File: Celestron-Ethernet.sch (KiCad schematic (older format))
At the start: 59 parts, among them J1 USB_B_Micro, J2 6P6C, J3 RJ45_Abracon_ARJP11A-MASA-B-A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, SW1 SW_SPDT, U1 ATmega32U4-AU, U2 LP2985-5.0, U3 LP2985-3.3, U4 W5500, Y1 16MHz, Y2 25MHz

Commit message: Initial routing
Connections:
- net labels added: 12V
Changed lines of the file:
@@
 Wire Wire Line
 	1750 2450 2550 2450
+Text Label 4450 5150 0    50   ~ 0
+12V
 $EndSCHEMATC

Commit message: bypass caps
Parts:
- added C15: 10uF, Capacitor_SMD:C_0603_1608Metric, symbol Device:C_Small
- added C16, C18, C20, C21, C24, C25, C26: 100nF, Capacitor_SMD:C_0603_1608Metric, symbol Device:C_Small
- added C27: 1nF/2KV, Capacitor_SMD:C_0603_1608Metric, symbol Device:C_Small
- added FB1: HH-1M1608-121JT, Inductor_SMD:L_0603_1608Metric, symbol Device:Ferrite_Bead_Small
- R18: value 12K4 -> 12.4K
- renumbered C8 to C10, C10 to C11, C15 to C17, C16 to C19, C17 to C22, C18 to C23, C11 to C5, C9 to C6, C5 to C7, C6 to C8, C7 to C9
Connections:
- net labels added: +3.3VA, GNDPWR
- wire segments 240 -> 282
- no-connect marks 29 -> 28
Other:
- moved on the sheet: C1, C10, C11, C12, C13, C14, C17, C19, C2, C22, C23, C3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

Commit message: corrected w5500 schematic, added mounting holes
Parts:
- removed JP1: USB PWR, Connector_PinHeader_2.54mm:PinHeader_1x02_P2.54mm_Vertical, symbol Jumper:Jumper_2_Open
- removed SW1: SW_SPDT, Button_Switch_THT:SW_E-Switch_EG1224_SPDT_Angled, symbol Switch:SW_SPDT
- added H1, H2, H3, H4: MountingHole, MountingHole:MountingHole_3.2mm_M3, symbol Mechanical:MountingHole
- added R17: 1M, Resistor_SMD:R_0603_1608Metric, symbol Device:R_Small
- added SW1: SW_DIP_x02, Button_Switch_SMD:SW_DIP_SPSTx02_Slide_9.78x7.26mm_W8.61mm_P2.54mm, symbol Switch:SW_DIP_x02
- FB1: value HH-1M1608-121JT -> 60 ohm/100MHz; MPN (none) -> BLM18PG600SN1D; Manufacturer (none) -> Murata
- renumbered C23 to C10, C13 to C11, C14 to C12, C27 to C13, C15 to C14, C16 to C15, C18 to C16, C20 to C17, C21 to C18, C24 to C19, C25 to C20, C26 to C21, C5 to C22, C6 to C23, C7 to C24, C8 to C25, C11 to C26, C12 to C27, C17 to C3, C9 to C4, C19 to C5, C10 to C6, C22 to C7, C3 to C8, C4 to C9, J3 to J2, J2 to J3, R8 to R1, R20 to R10, R26 to R11, R23 to R12, R24 to R13, R25 to R14, R1 to R15, R2 to R16, R21 to R18, R6 to R19, R10 to R2, R7 to R20, R9 to R21, R11 to R22, R13 to R23, R15 to R24, R22 to R25, R18 to R26, R19 to R27, R12 to R3, R14 to R4, R16 to R5, R17 to R6, R3 to R7, R4 to R8, R5 to R9, U4 to U1, U1 to U2, U2 to U3, U3 to U4
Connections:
- net labels added: DCHP_ENA, USB_PWR
- wire segments 282 -> 294
- no-connect marks 28 -> 27
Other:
- moved on the sheet: C10, C11, C12, C13, C4, C5, C6, C7, FB1, R1, R10, R11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

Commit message: traces complete
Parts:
- removed C8, C9: 100nF, Capacitor_SMD:C_0603_1608Metric, symbol Device:C_Small
- removed D2: Grn, LED_SMD:LED_0603_1608Metric, symbol Device:LED_Small
- removed J1: USB_B_Micro, Connector_USB:USB_Micro-B_GCT_USB3076-30-A, symbol Connector:USB_B_Micro
- removed J2: RJ45_Abracon_ARJP11A-MASA-B-A-EMU2, Connector_RJ:RJ45_Abracon_ARJP11A-MA_Horizontal, symbol Connector:RJ45_Abracon_ARJP11A-MASA-B-A-EMU2
- removed R15, R16: 22R, Resistor_SMD:R_0603_1608Metric, symbol Device:R_Small
- removed R8, R9: 330R, Resistor_SMD:R_0603_1608Metric, symbol Device:R_Small
- removed SW1: SW_DIP_x02, Button_Switch_SMD:SW_DIP_SPSTx02_Slide_9.78x7.26mm_W8.61mm_P2.54mm, symbol Switch:SW_DIP_x02
- removed U2: ATmega32U4-AU, Package_QFP:TQFP-44_10x10mm_P0.8mm, symbol MCU_Microchip_ATmega:ATmega32U4-AU
- added C1, C10, C22, C23: 100nF, Capacitor_SMD:C_0603_1608Metric, symbol Device:C_Small
- added C24: 10uF, Capacitor_SMD:C_0603_1608Metric, symbol Device:C_Small
- added J1: FTDI, Connector_PinHeader_2.54mm:PinHeader_1x06_P2.54mm_Horizontal, symbol Connector_Generic:Conn_01x06
- added J2: RJ45_Amphenol_RJMG1BD3B8K1ANR, Connector_RJ:RJ45_Amphenol_RJMG1BD3B8K1ANR, symbol Connector:RJ45_Amphenol_RJMG1BD3B8K1ANR
- added R10: 330R, Resistor_SMD:R_0603_1608Metric, symbol Device:R_Small
- added SW1: SW_Push, Button_Switch_SMD:SW_SPST_FSMSM, symbol Switch:SW_Push
- added SW2: DHCP, Button_Switch_THT:SW_E-Switch_EG1224_SPDT_Angled, symbol Switch:SW_SPDT
- added U2: ATmega328-AU, Package_QFP:TQFP-32_7x7mm_P0.8mm, symbol MCU_Microchip_ATmega:ATmega328-AU_(alt)
- C11: renamed from C13; footprint Capacitor_SMD:C_0603_1608Metric -> Capacitor_SMD:C_1206_3216Metric; MPN (none) -> C1206C102KGRACTU; Manufacturer (none) -> KEMET
- C12: MPN (none) -> GRM188R61C475KE11D; Manufacturer (none) -> Murata
- C2: renamed from C1; value 22pF -> 18pF
- C21: renamed from C14; MPN (none) -> GRM188R61C106MA73D; Manufacturer (none) -> Murata
- C3: renamed from C5; MPN (none) -> C0603C682J4HACTU; Manufacturer (none) -> KEMET
- C4: renamed from C2; value 22pF -> 18pF
- C5: renamed from C7; MPN (none) -> C0603C682J4HACTU; Manufacturer (none) -> KEMET
- D1: value Ylw -> Red
- D2: renamed from D3; footprint Diode_SMD:D_SOD-123 -> Diode_SMD:D_SOD-323F
- R11: renamed from R14; value 49R9 -> 82R
- R12: renamed from R13; value 49R9 -> 82R
- U1: MPN (none) -> W5500
- Y1: MPN (none) -> 406C35D16M00000; Manufacturer (none) -> CTS
- Y2: MPN (none) -> 406C35D25M00000; Manufacturer (none) -> CTS
- renumbered C11 to C13, C21 to C14, C20 to C15, C19 to C16, C18 to C17, C17 to C18, C16 to C19, C15 to C20, C27 to C25, C25 to C27, C24 to C28, C23 to C29, C22 to C30, C4 to C6, C6 to C7, C3 to C8, C10 to C9, D4 to D3, R6 to R1, R17 to R13, R7 to R14, R18 to R15, R25 to R16, R24 to R17, R23 to R18, R22 to R19, R5 to R2, R21 to R20, R20 to R21, R19 to R22, R26 to R23, R27 to R24, R4 to R3, R3 to R4, R2 to R5, R1 to R6, R12 to R7, R11 to R8, R10 to R9, U4 to U3, U3 to U4
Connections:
- net labels added: +12V, D8, DTR, LEDG_A, LEDG_K, LEDY_A, LEDY_K, MISO, MOSI, RCT, RD+, RD-, RXI, SCK, TCT, TD+, TD-, TXO
- net labels removed: 12V, DCHP_ENA, USB_PWR
- wire segments 294 -> 295
- no-connect marks 27 -> 21
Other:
- moved on the sheet: C11, C12, C13, C14, C15, C16, C17, C18, C19, C2, C20, C21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

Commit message: silkscreen
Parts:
- D3: value Red -> Blu
- J2: MPN (none) -> RJMG1BD3B8K1ANR; Manufacturer (none) -> Amphenol
- J3: MPN (none) -> 54601-906001WPLF; Manufacturer (none) -> Amphenol
- U1: Manufacturer (none) -> Wiznet
- U2: value ATmega328-AU -> ATmega328P-AU; Manufacturer (none) -> Atmel
- U3, U4: Manufacturer (none) -> Texas Instruments
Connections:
- net TXO: no longer J1.5 (Pin_5)
- net LINKLED: now reaches R15.2, U1.25 (LINKLED)
- net ACTLED: now reaches R16.2, U1.27 (ACTLED)
- net RXN: now reaches C5.2, R12.1, U1.5 (RXN)
- net RXP: now reaches C3.1, R11.1, U1.6 (RXP)
- net ~RST: now reaches C10.1, R14.2, SW1.2, U2.29 (~RESET~/PC6)
- net TX: now reaches D2.1 (K), U2.31 (PD1)
- net TX: now also J1.5 (Pin_5)
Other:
- moved on the sheet: C11
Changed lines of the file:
@@
 F 3 "http://wizwiki.net/wiki/lib/exe/fetch.php/products:w5500:w5500_ds_v109e.pdf" H 5600 3350 50  0001 C CNN
 F 4 "W5500" H 5600 2350 50  0001 C CNN "MPN"
+F 5 "Wiznet" H 5600 2350 50  0001 C CNN "Manufacturer"
 	1    5600 2350
 	-1   0    0    -1
@@
 F 2 "Connector_RJ:RJ12_Amphenol_54601" V 10650 4925 50  0001 C CNN
 F 3 "~" V 10650 4925 50  0001 C CNN
+F 4 "54601-906001WPLF" H 10650 4900 50  0001 C CNN "MPN"
+F 5 "Amphenol" H 10650 4900 50  0001 C CNN "Manufacturer"
 	1    10650 4900
 	-1   0    0    1
@@
 F 2 "Package_TO_SOT_SMD:SOT-23-5" H 3050 7175 50  0001 C CNN
 F 3 "http://www.ti.com/lit/ds/symlink/lp2985.pdf" H 3050 6850 50  0001 C CNN
+F 4 "Texas Instruments" H 3050 6850 50  0001 C CNN "Manufacturer"
 	1    3050 6850
 	-1   0    0    -1
@@
 F 2 "Package_TO_SOT_SMD:SOT-23-5" H 5050 7175 50  0001 C CNN
 F 3 "http://www.ti.com/lit/ds/symlink/lp2985.pdf" H 5050 6850 50  0001 C CNN
+F 4 "Texas Instruments" H 5050 6850 50  0001 C CNN "Manufacturer"
 	1    5050 6850
 	1    0    0    -1
@@
 U 1 1 61996150
 P 9850 2100
-F 0 "Y1" V 9896 2012 50  0000 R CNN
-F 1 "16MHz" V 9805 2012 50  0000 R CNN
+F 0 "Y1" V 9800 2350 50  0000 R CNN
+F 1 "16MHz" V 9900 2450 50  0000 R CNN
 F 2 "Crystal:Crystal_SMD_0603-2Pin_6.0x3.5mm" H 9850 2100 50  0001 C CNN
 F 3 "~" H 9850 2100 50  0001 C CNN
@@
 P 6300 5750
 F 0 "D3" V 6346 5680 50  0000 R CNN
-F 1 "Red" V 6255 5680 50  0000 R CNN
+F 1 "Blu" V 6255 5680 50  0000 R CNN
 F 2 "LED_SMD:LED_0603_1608Metric" V 6300 5750 50  0001 C CNN
 F 3 "~" V 6300 5750 50  0001 C CNN
@@
 U 1 1 61B66D07
 P 6800 3750
-F 0 "R22" H 6700 3600 50  0000 L CNN
+F 0 "R22" V 6750 3500 50  0000 L CNN
 F 1 "10K" V 6750 3850 50  0000 L CNN
 F 2 "Resistor_SMD:R_0603_1608Metric" H 6800 3750 50  0001 C CNN
@@
 U 1 1 61B6C10C
 P 6700 3750
-F 0 "R21" H 6600 3600 50  0000 L CNN
+F 0 "R21" V 6650 3500 50  0000 L CNN
 F 1 "10K" V 6650 3850 50  0000 L CNN
 F 2 "Resistor_SMD:R_0603_1608Metric" H 6700 3750 50  0001 C CNN
@@
 U 1 1 61B6CBA5
 P 6600 3750
-F 0 "R20" H 6500 3600 50  0000 L CNN
+F 0 "R20" V 6550 3500 50  0000 L CNN
 F 1 "10K" V 6550 3850 50  0000 L CNN
 F 2 "Resistor_SMD:R_0603_1608Metric" H 6600 3750 50  0001 C CNN
@@
 U 1 1 61B6D7AE
 P 6500 3750
-F 0 "R19" H 6400 3600 50  0000 L CNN
+F 0 "R19" V 6450 3500 50  0000 L CNN
 F 1 "10K" V 6450 3850 50  0000 L CNN
 F 2 "Resistor_SMD:R_0603_1608Metric" H 6500 3750 50  0001 C CNN
@@
 U 1 1 61B6E19D
 P 6400 3750
-F 0 "R18" H 6300 3600 50  0000 L CNN
+F 0 "R18" V 6350 3500 50  0000 L CNN
 F 1 "10K" V 6350 3850 50  0000 L CNN
 F 2 "Resistor_SMD:R_0603_1608Metric" H 6400 3750 50  0001 C CNN
@@
 U 1 1 61B6EB4B
 P 6300 3750
-F 0 "R17" H 6200 3600 50  0000 L CNN
+F 0 "R17" V 6250 3500 50  0000 L CNN
 F 1 "10K" V 6250 3850 50  0000 L CNN
 F 2 "Resistor_SMD:R_0603_1608Metric" H 6300 3750 50  0001 C CNN
@@
 U 1 1 61C89AFA
 P 3400 2050
-F 0 "C3" H 3550 1950 50  0000 C CNN
-F 1 "6.8nF" H 3600 2050 50  0000 C CNN
+F 0 "C3" H 3350 2000 50  0000 C CNN
+F 1 "6.8nF" H 3400 2150 50  0000 C CNN
 F 2 "Capacitor_SMD:C_0603_1608Metric" H 3400 2050 50  0001 C CNN
 F 3 "~" H 3400 2050 50  0001 C CNN
@@
 U 1 1 61D2F178
 P 3400 2250
-F 0 "C5" H 3250 2350 50  0000 C CNN
-F 1 "6.8nF" H 3200 2250 50  0000 C CNN
+F 0 "C5" H 3450 2300 50  0000 C CNN
+F 1 "6.8nF" H 3400 2150 50  0000 C CNN
 F 2 "Capacitor_SMD:C_0603_1608Metric" H 3400 2250 50  0001 C CNN
 F 3 "~" H 3400 2250 50  0001 C CNN
@@
 U 1 1 6226E112
 P 4800 4150
-F 0 "C12" H 4900 3950 50  0000 R CNN
-F 1 "4.7uF" H 5000 4050 50  0000 R CNN
+F 0 "C12" H 4950 4100 50  0000 R CNN
+F 1 "4.7uF" H 5000 4250 50  0000 R CNN
 F 2 "Capacitor_SMD:C_0603_1608Metric" H 4800 4150 50  0001 C CNN
 F 3 "~" H 4800 4150 50  0001 C CNN
@@
 U 1 1 622E057D
 P 5000 4150
-F 0 "C13" H 5200 4050 50  0000 R CNN
-F 1 "10nF" H 5300 4150 50  0000 R CNN
+F 0 "C13" H 5150 4100 50  0000 R CNN
+F 1 "10nF" H 5200 4250 50  0000 R CNN
 F 2 "Capacitor_SMD:C_0603_1608Metric" H 5000 4150 50  0001 C CNN
 F 3 "~" H 5000 4150 50  0001 C CNN
@@
 L power:GND #PWR018
 U 1 1 61C1314F
-P 1200 3450
-F 0 "#PWR018" H 1200 3200 50  0001 C CNN
-F 1 "GND" H 1205 3277 50  0000 C CNN
-F 2 "" H 1200 3450 50  0001 C CNN
-F 3 "" H 1200 3450 50  0001 C CNN
-	1    1200 3450
+P 1550 3450
+F 0 "#PWR018" H 1550 3200 50  0001 C CNN
+F 1 "GND" H 1555 3277 50  0000 C CNN
+F 2 "" H 1550 3450 50  0001 C CNN
+F 3 "" H 1550 3450 50  0001 C CNN
+	1    1550 3450
 	-1   0    0    -1
 $EndComp
@@
 L Device:C_Small C11
 U 1 1 61C13AF2
-P 950 3300
-F 0 "C11" V 800 3300 50  0000 C CNN
-F 1 "1nF/2KV" V 700 3300 50  0000 C CNN
-F 2 "Capacitor_SMD:C_1206_3216Metric" H 950 3300 50  0001 C CNN
-F 3 "~" H 950 3300 50  0001 C CNN
-F 4 "C1206C102KGRACTU" H 950 3300 50  0001 C CNN "MPN"
-F 5 "KEMET" H 950 3300 50  0001 C CNN "Manufacturer"
-	1    950  3300
+P 1150 3300
+F 0 "C11" V 1000 3300 50  0000 C CNN
+F 1 "1nF/2KV" V 900 3300 50  0000 C CNN
+F 2 "Capacitor_SMD:C_1206_3216Metric" H 1150 3300 50  0001 C CNN
+F 3 "~" H 1150 3300 50  0001 C CNN
+F 4 "C1206C102KGRACTU" H 1150 3300 50  0001 C CNN "MPN"
+F 5 "KEMET" H 1150 3300 50  0001 C CNN "Manufacturer"
+	1    1150 3300
 	0    1    -1   0
 $EndComp
@@
 	650  3450 650  3300
 Wire Wire Line
-	650  3300 850  3300
-Wire Wire Line
-	1200 3450 1200 3300
-Wire Wire Line
-	1200 3300 1050 3300
+	650  3300 1050 3300
+Wire Wire Line
+	1550 3450 1550 3300
 $Comp
 L power:PWR_FLAG #FLG02
 U 1 1 61CC0CBD
-P 2950 4550
-F 0 "#FLG02" H 2950 4625 50  0001 C CNN
-F 1 "PWR_FLAG" H 2950 4723 50  0000 C CNN
-F 2 "" H 2950 4550 50  0001 C CNN
-F 3 "~" H 2950 4550 50  0001 C CNN
-	1    2950 4550
+P 2950 4650
+F 0 "#FLG02" H 2950 4725 50  0001 C CNN
+F 1 "PWR_FLAG" H 2950 4823 50  0000 C CNN
+F 2 "" H 2950 4650 50  0001 C CNN
+F 3 "~" H 2950 4650 50  0001 C CNN
+	1    2950 4650
 	-1   0    0    1
 $EndComp
 Wire Wire Line
-	2950 4550 3200 4550
-Connection ~ 3200 4550
+	2950 4650 3200 4650
 $Comp
 L power:PWR_FLAG #FLG01
@@
 Connection ~ 650  3300
 Wire Wire Line
-	3750 2700 3750 2800
+	3750 2700 3750 2750
 $Comp
 L power:GND #PWR015
@@
 P 8850 2650
 F 0 "U2" H 8850 2800 50  0000 C CNN
-F 1 "ATmega328-AU" H 8800 2650 50  0000 C CNN
+F 1 "ATmega328P-AU" H 8800 2650 50  0000 C CNN
 F 2 "Package_QFP:TQFP-32_7x7mm_P0.8mm" H 8850 2650 50  0001 C CIN
 F 3 "http://ww1.microchip.com/downloads/en/DeviceDoc/Atmel-8025-8-bit-AVR-Microcontroller-ATmega48P-88P-168P_Datasheet.pdf" H 8850 2650 50  0001 C CNN
 F 4 "ATMEGA328-AU" H 8850 2650 50  0001 C CNN "MPN"
+F 5 "Atmel" H 8850 2650 50  0001 C CNN "Manufacturer"
 	1    8850 2650
 	-1   0    0    -1
@@
 DTR
 Text Label 10800 900  2    50   ~ 0
-TXO
+TX
 Text Label 10800 1000 2    50   ~ 0
 RXI
@@
 	1    0    0    -1
 $EndComp
-Text Label 7500 1450 2    50   ~ 0
+Text Label 7250 1450 2    50   ~ 0
 SCK
-Text Label 7500 1550 2    50   ~ 0
+Text Label 7250 1550 2    50   ~ 0
 MISO
-Text Label 7500 1650 2    50   ~ 0
+Text Label 7250 1650 2    50   ~ 0
 MOSI
 Wire Wire Line
@@
 F 2 "Connector_RJ:RJ45_Amphenol_RJMG1BD3B8K1ANR" H 1550 2950 50  0001 C CNN
 F 3 "https://www.amphenolcanada.com/ProductSearch/Drawings/AC/RJMG1BD3B8K1ANR.PDF" H 1550 3050 50  0001 C CNN
+F 4 "RJMG1BD3B8K1ANR" H 1550 2250 50  0001 C CNN "MPN"
+F 5 "Amphenol" H 1550 2250 50  0001 C CNN "Manufacturer"
 	1    1550 2250
 	-1   0    0    -1
@@
 	650  3000 650  3300
 Wire Wire Line
-	1200 3300 1550 3300
-Wire Wire Line
 	1550 3300 1550 2950
-Connection ~ 1200 3300
 Text Label 2600 2050 0    50   ~ 0
 RD+
@@
 Wire Wire Line
 	2450 2150 3050 2150
-Wire Wire Line
-	3050 2150 3050 2700
-Wire Wire Line
-	3050 2700 3700 2700
-Connection ~ 3700 2700
 Wire Wire Line
 	3700 1550 3700 1950
@@
 Text Label 8850 5200 0    50   ~ 0
 D8
+Connection ~ 1550 3300
+Wire Wire Line
+	1250 3300 1550 3300
+Wire Wire Line
+	3750 2750 3050 2750
+Connection ~ 3750 2750
+Wire Wire Line
+	3750 2750 3750 2800
+Wire Wire Line
+	3050 2150 3050 2750
+Text Label 4250 2250 0    50   ~ 0
+RXN
+Text Label 9750 2950 0    50   ~ 0
+~RST
+Connection ~ 3200 4650
+Text Label 4000 3450 0    50   ~ 0
+LINKLED
+Text Label 4000 3600 0    50   ~ 0
+ACTLED
+Text Label 4250 2050 0    50   ~ 0
+RXP
+Text Label 8000 3800 0    50   ~ 0
+TX
 $EndSCHEMATC

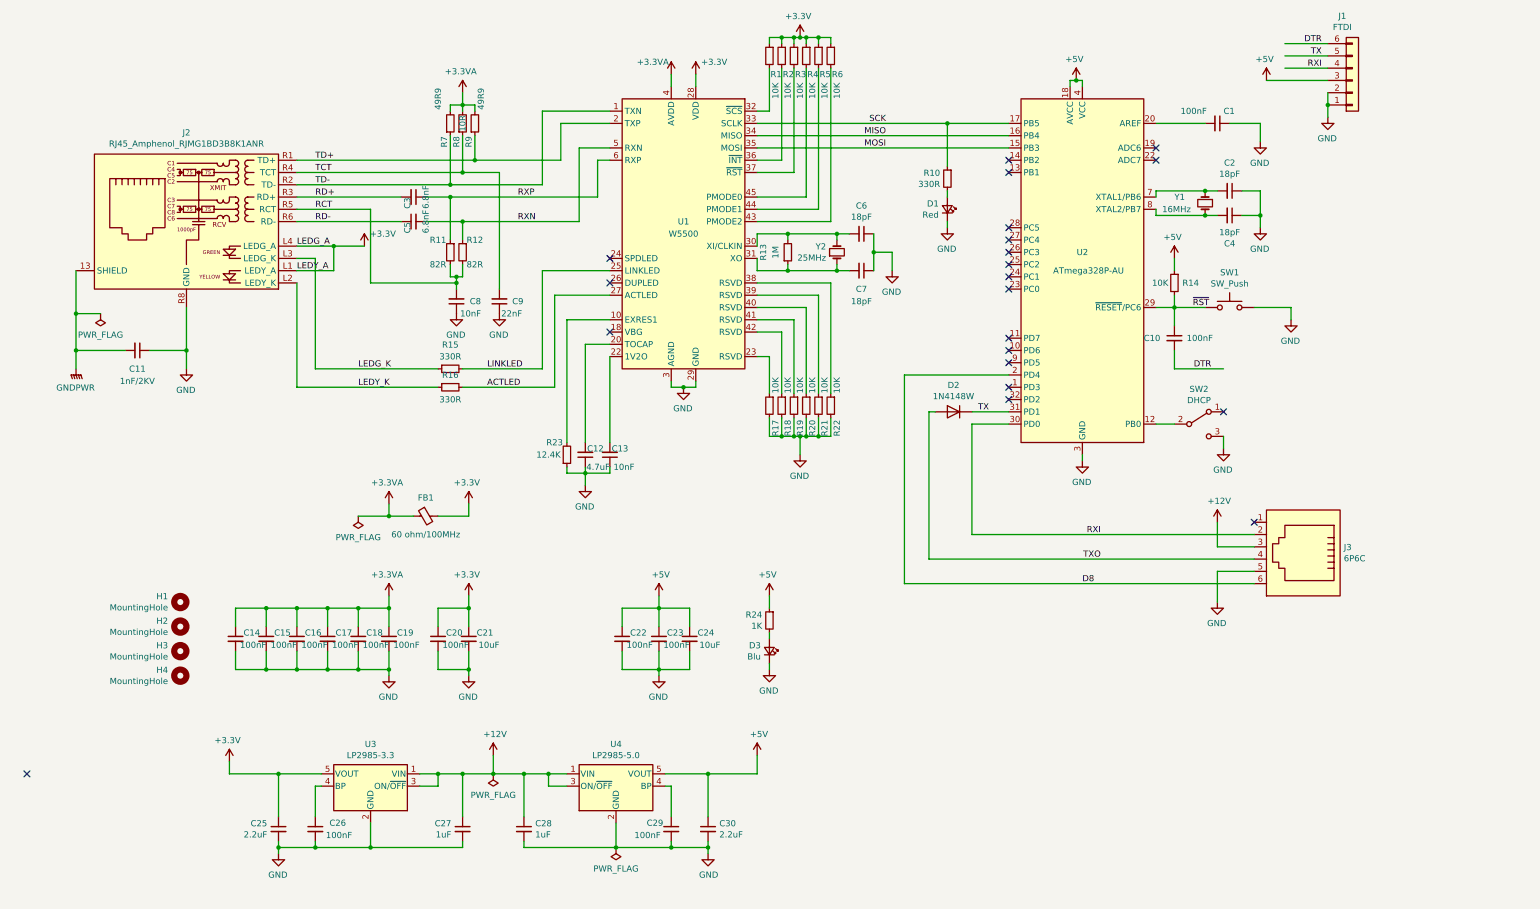
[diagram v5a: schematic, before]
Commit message: schematic fixes, moved copper planes
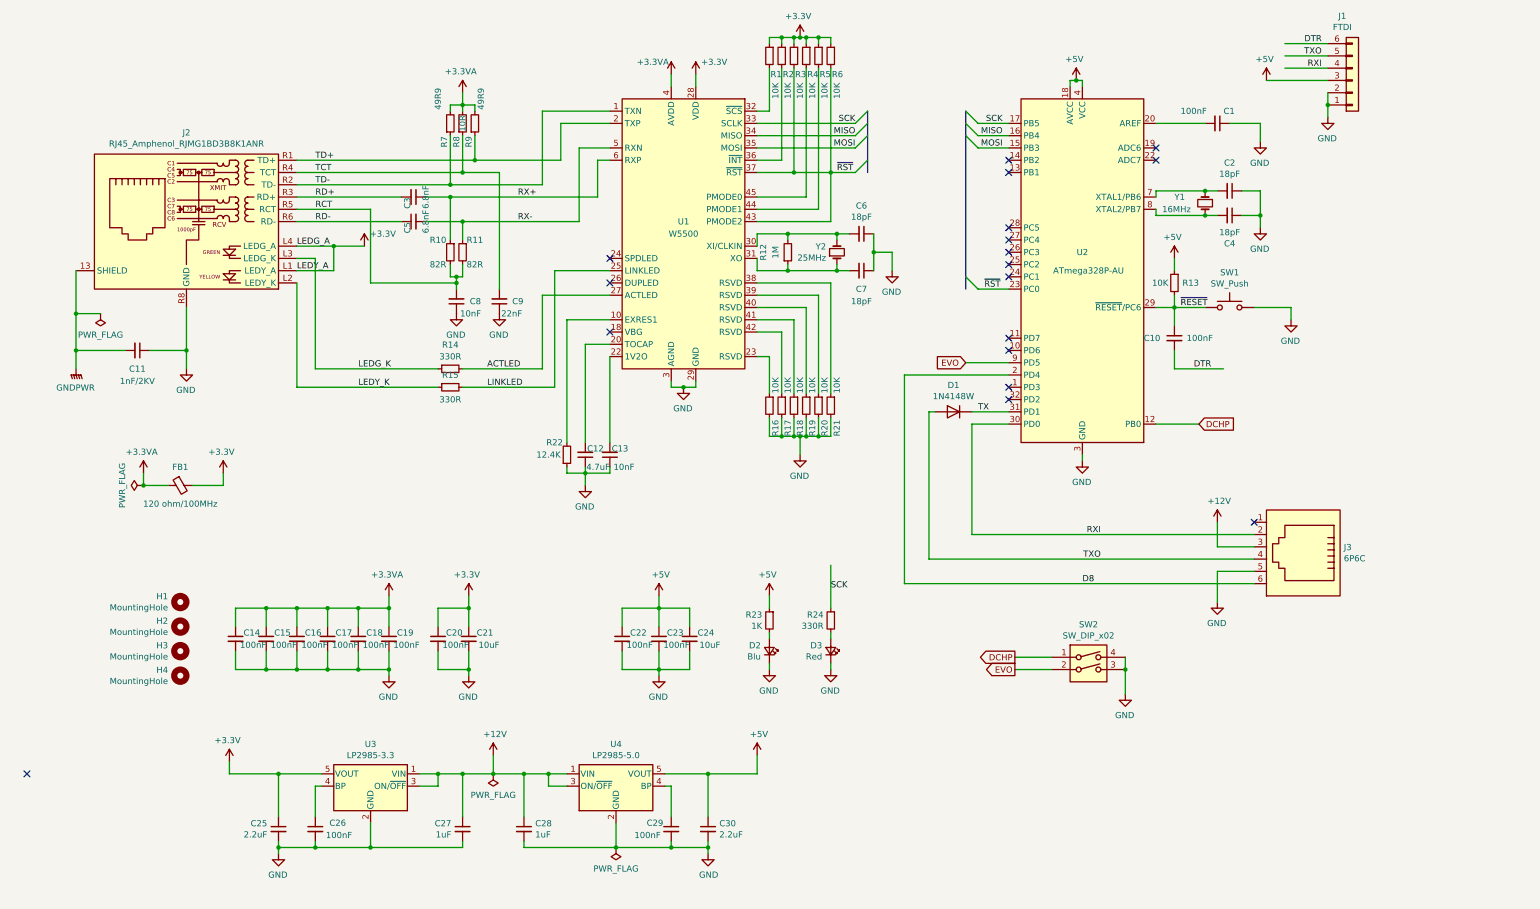
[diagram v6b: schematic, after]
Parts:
- removed SW2: DHCP, Button_Switch_THT:SW_E-Switch_EG1224_SPDT_Angled, symbol Switch:SW_SPDT
- added SW2: SW_DIP_x02, Button_Switch_SMD:SW_DIP_SPSTx02_Slide_6.7x6.64mm_W8.61mm_P2.54mm_LowProfile, symbol Switch:SW_DIP_x02
- FB1: value 60 ohm/100MHz -> 120 ohm/100MHz; MPN BLM18PG600SN1D -> FBMH1608HL121-T; Manufacturer Murata -> Tayo Yuden
- renumbered D2 to D1, D3 to D2, D1 to D3, R11 to R10, R12 to R11, R13 to R12, R14 to R13, R15 to R14, R16 to R15, R17 to R16, R18 to R17, R19 to R18, R20 to R19, R21 to R20, R22 to R21, R23 to R22, R24 to R23, R10 to R24
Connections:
- net ACTLED: now also R14.2; no longer R15.2
- net GND: now also SW2.3, SW2.4
- net LINKLED: now also R15.2; no longer R14.2
- net TX: no longer J1.5 (Pin_5)
- net TXO: now also J1.5 (Pin_5)
- net ~RST: now also R3.2, R6.2, U1.37 (~RST), U1.43 (PMODE2), U2.23 (PC0); no longer C10.1, R13.2, SW1.2, U2.29 (~RESET~/PC6)
- net DCHP: now reaches U2.12 (PB0)
- net DCHP: now also SW2.1
- net EVO: now reaches U2.9 (PD5)
- net EVO: now also SW2.2
- net RXN renamed RX-
- net RXP renamed RX+
- new net ~RESET: C10.1, R13.2, SW1.2, U2.29 (~RESET~/PC6)
- no-connect marks 21 -> 18
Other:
- moved on the sheet: D3, FB1, R24
